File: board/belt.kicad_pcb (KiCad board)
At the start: 2 copper layers, 56.5 x 48.2 mm, 25 parts, among them J1 USB_B_Micro, J2 USB_B_Micro, J3 USB_B_Micro, J4 USB_B_Micro, P1 3352T-1-103LF, Q1 BSS138, Q2 BSS138, SW1 SW_SPST, SW2 SW_Push, U1 Teensy4.0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

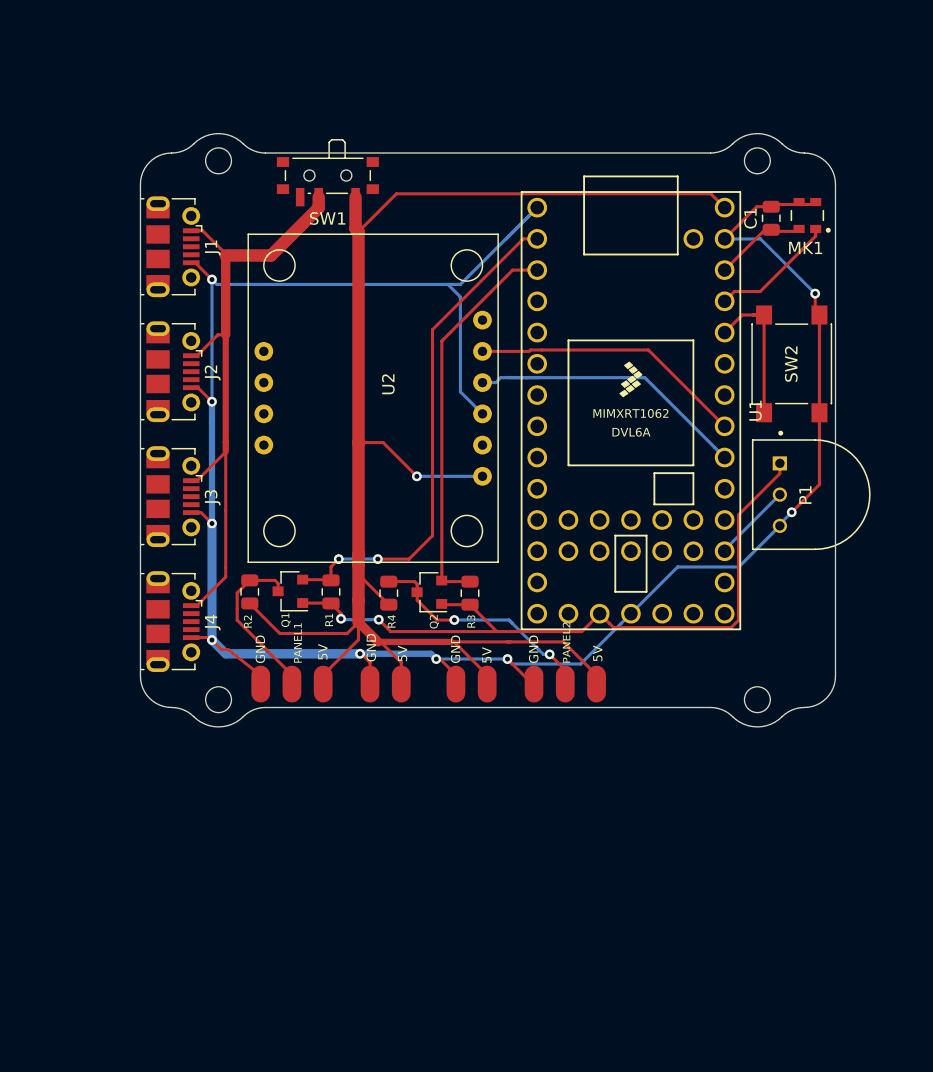
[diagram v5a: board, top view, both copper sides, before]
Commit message: mostly done with next board iteration, except for new microphone; use new microphone in software to draw a rainbow fft that is super fun to play with
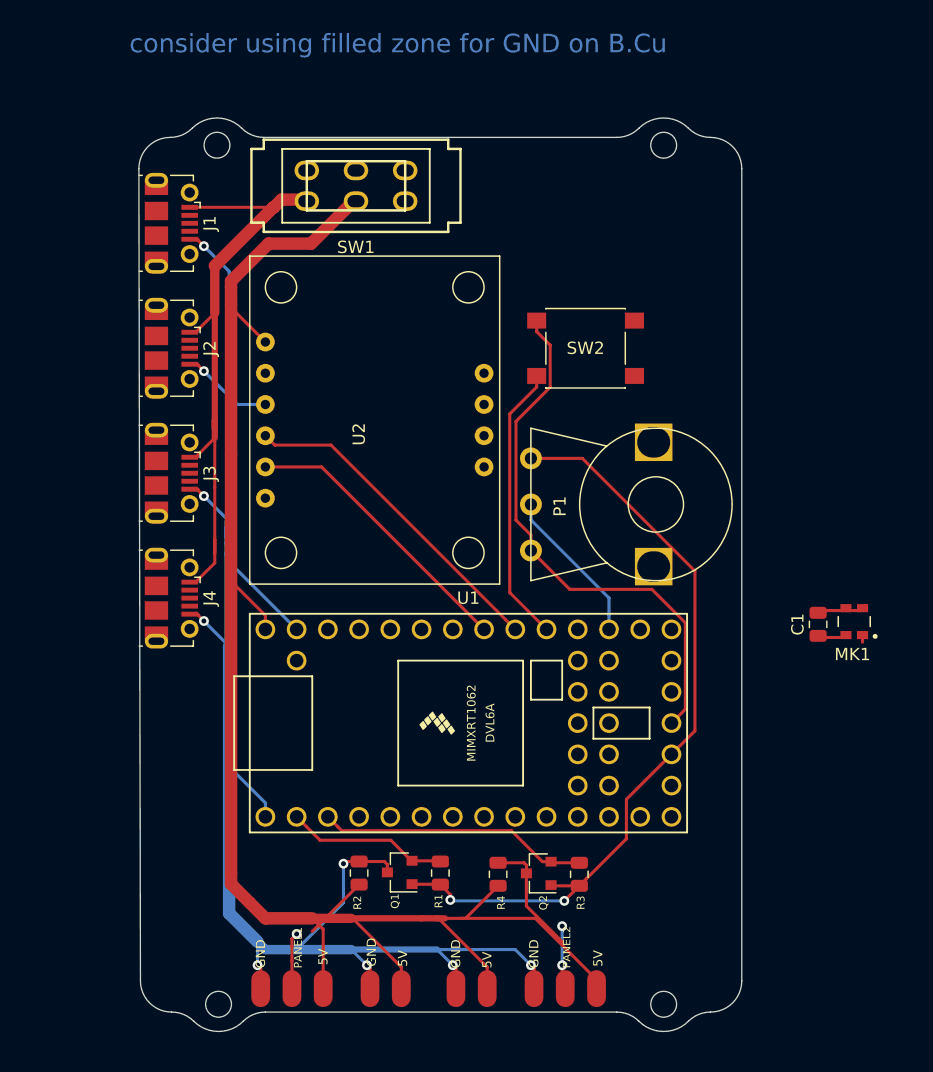
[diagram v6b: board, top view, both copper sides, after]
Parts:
- removed the REF** at (169.5, 70.5)
- removed the REF** at (125.7, 70.5)
- removed the REF** at (125.7, 114.3)
- added REF**: MountingHole_2.1mm, MountingHole:MountingHole_2.1mm, F.Cu at (161.9, 69.2)
- added REF**: MountingHole_2.1mm, MountingHole:MountingHole_2.1mm, F.Cu at (125.6, 69.2)
- added REF**: MountingHole_2.1mm, MountingHole:MountingHole_2.1mm, F.Cu at (125.7, 139.1)
- P1: footprint 3352T-1-103LF:TRIM_3352T-1-103LF -> Potentiometer_THT:PDB12-H
- SW1: value SW_SPST -> SW_DPDT; footprint Button_Switch_SMD:SW_SPDT_PCM12 -> engstad:slide-switch-MFS201N-9-Z
- moved C1 33.2 mm to (174.5, 108.2)
- moved MK1 33.2 mm to (177.4, 108.0)
- moved U1 28.6 mm to (146.1, 116.2), turned to 0 degrees
- moved REF** 25.9 mm to (161.9, 139.1)
- moved PANEL1 24.8 mm to (131.7, 137.8)
- moved PANEL2 24.8 mm to (153.9, 137.8)
- moved PANEL_PWR1 24.8 mm to (139.3, 137.8)
- moved PANEL_PWR2 24.8 mm to (146.3, 137.8)
- moved R3 24.5 mm to (155.1, 128.5)
- moved Q1 24.5 mm to (140.5, 128.3)
- moved Q2 24.5 mm to (151.8, 128.4)
- moved R4 24.5 mm to (148.5, 128.5)
- moved R1 24.5 mm to (143.8, 128.4)
- moved R2 24.5 mm to (137.2, 128.4)
- moved P1 23.1 mm to (151.1, 98.4)
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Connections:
- C1 pad 1: /MIC_PWR -> +3V3
- MK1 pad 4: /MIC_PWR -> +3V3
- SW1 pad 1: VDD -> VBUS
- SW1 pad 2: VBUS -> VDD
- SW1 pad 3: (no net) -> Net-(SW1-Pad3)
- U1 pad 21: Net-(U1-Pad21) -> /MICROPHONE
- U1 pad 24: Net-(U1-Pad24) -> /BUTTON
- U1 pad 29: /BUTTON -> Net-(U1-Pad29)
- U1 pad 30: /MICROPHONE -> Net-(U1-Pad30)
- U1 pad 31: /MIC_PWR -> Net-(U1-Pad31)
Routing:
- net /DATA1: track 41.2 -> 13.3 mm, vias 2 -> 0
- net VDD: track 129.2 -> 139.5 mm, vias 1 -> 0
- net /BUTTON: track 12.7 -> 22.8 mm
- net /DATA2: track 32.1 -> 22.1 mm
- net /MICROPHONE: track 10.2 -> 0.58 mm
- net +3V3: track 57.7 -> 66.1 mm
- net /MIC_PWR: track 7.38 -> 0.00 mm
- net /THUMBDIAL: track 6.46 -> 12.8 mm
- net Net-(PANEL1-Pad2): track 13.8 -> 18.7 mm, vias 0 -> 2
- net Net-(PANEL2-Pad2): track 19.3 -> 16.1 mm
- net /MOTION_SDA: track 25.1 -> 26.8 mm
- net VBUS: track 51.6 -> 53.3 mm
- net /MOTION_SCL: track 22.3 -> 23.3 mm
- net GND: track 186.4 -> 187.3 mm, vias 9 -> 8
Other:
- board size 56.5 x 48.2 mm -> 49 x 74.3 mm
- board text added: "consider using filled zone for GND on B.Cu"

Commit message: checkpoint for 3rd board layout with veritcal structure, two pots, and digital mic
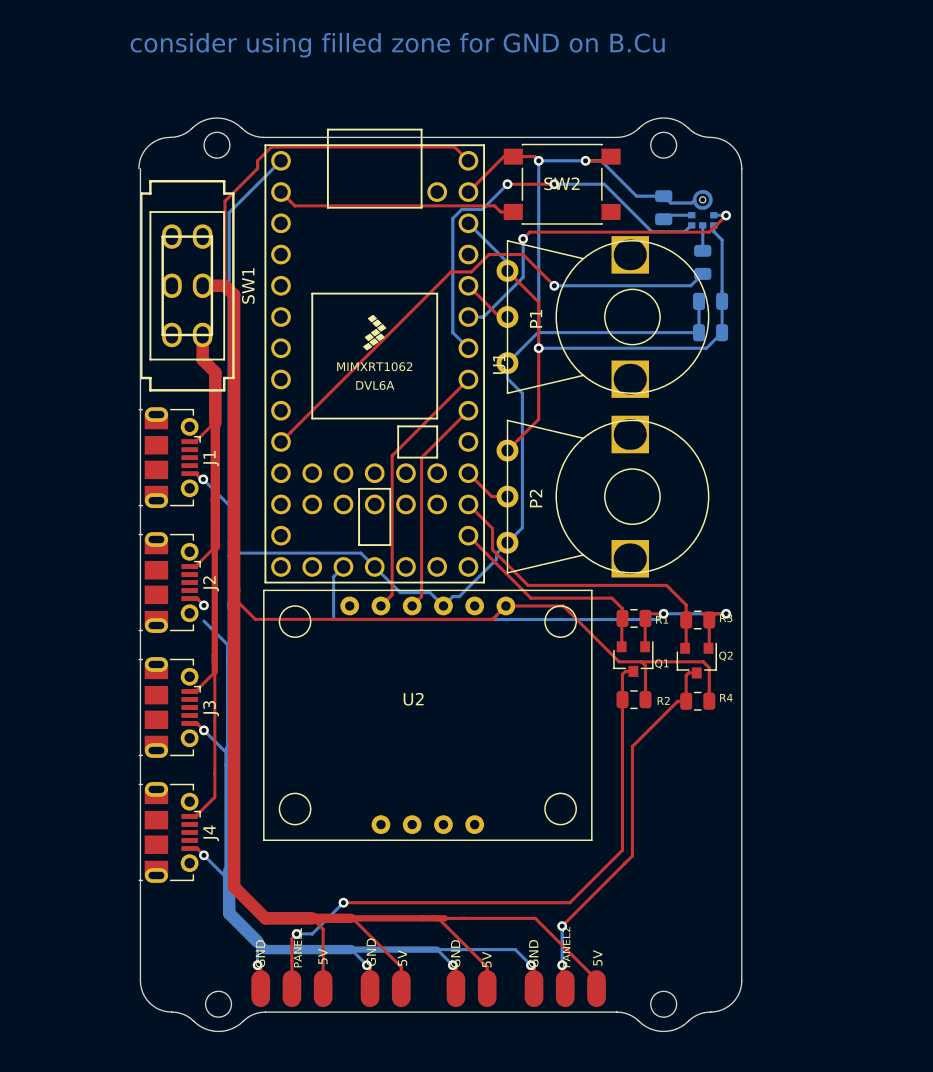
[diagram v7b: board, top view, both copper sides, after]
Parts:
- added C2: 220pF, Capacitor_SMD:C_0805_2012Metric, B.Cu at (165.7, 84.5)
- added P2: 3352T-1-103LF, Potentiometer_THT:PDB12-H, F.Cu at (149.2, 97.8)
- added R5: 10K, Resistor_SMD:R_0805_2012Metric, B.Cu at (161.9, 74.3)
- added R6: 68, Resistor_SMD:R_0805_2012Metric, B.Cu at (165.1, 78.7)
- C1: value 0.1µF -> 1uF; moved to B.Cu
- MK1: value SPW2430HR5H-B -> SPH0645LM4H-B; footprint SPW2430HR5H-B:MIC_SPW2430HR5H-B -> Mic-SPH0645LM4H-B:MIC_SPH0645LM4H-B; moved to B.Cu
- moved MK1 36.4 mm to (165.1, 73.7), turned to 0 degrees
- moved U1 30.2 mm to (138.4, 87.0), turned to 270 degrees
- moved C1 27.7 mm to (165.7, 81.9), turned to 0 degrees
- moved R2 26.4 mm to (159.5, 114.3), turned to 180 degrees
- moved R1 26.0 mm to (159.5, 107.7), turned to 180 degrees
- moved Q1 25.7 mm to (159.5, 111.0), turned to 270 degrees
- moved U2 24.5 mm to (142.9, 115.6), turned to 180 degrees
- moved R3 22.8 mm to (164.7, 107.8), turned to 180 degrees
- moved Q2 21.5 mm to (164.6, 111.1), turned to 270 degrees
- moved R4 21.5 mm to (164.7, 114.4), turned to 180 degrees
- moved J2 19.1 mm to (121.9, 104.8)
- moved J1 19.0 mm to (121.9, 94.6)
- moved J3 19.0 mm to (121.9, 114.9)
- moved J4 19.0 mm to (121.9, 125.1)
- moved SW1 15.9 mm to (123.2, 80.6), turned to 90 degrees
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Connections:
- C1 pad 1: +3V3 -> GND
- C1 pad 2: GND -> +3.3VA
- MK1 pad 1: /MICROPHONE -> /MIC_LRCLK
- MK1 pad 2: GND -> Net-(MK1-Pad2)
- MK1 pad 4: +3V3 -> /MIC_BCLK
- P1 pad 1: +3V3 -> +3.3VA
- P1 pad 2: /THUMBDIAL -> /THUMBDIAL1
- U1 pad 10: Net-(U1-Pad10) -> /MIC_DATA_IN
- U1 pad 2: /DATA1 -> /BUTTON
- U1 pad 21: /MICROPHONE -> /DATA1
- U1 pad 22: /THUMBDIAL -> /DATA2
- U1 pad 23: Net-(U1-Pad23) -> /THUMBDIAL2
- U1 pad 24: /BUTTON -> Net-(U1-Pad24)
- U1 pad 27: Net-(U1-Pad27) -> /MIC_LRCLK
- U1 pad 28: Net-(U1-Pad28) -> /MIC_BCLK
- U1 pad 29: Net-(U1-Pad29) -> /THUMBDIAL1
- U1 pad 3: /DATA2 -> Net-(U1-Pad3)
- U1 pad 31: Net-(U1-Pad31) -> +3.3VA
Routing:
- net +3.3VA: track 0.00 -> 46.3 mm, vias 0 -> 1
- net VDD: track 139.5 -> 185.1 mm
- net /MIC_DATA_IN: track 0.00 -> 42.1 mm, vias 0 -> 1
- net GND: track 187.3 -> 225.1 mm, vias 8 -> 10
- net /MIC_LRCLK: track 0.00 -> 33.5 mm, vias 0 -> 2
- net Net-(PANEL1-Pad2): track 18.7 -> 50.0 mm
- net /MIC_BCLK: track 0.00 -> 27.2 mm, vias 0 -> 2
- net +3V3: track 66.1 -> 45.5 mm
- net Net-(PANEL2-Pad2): track 16.1 -> 32.3 mm
- net /THUMBDIAL: track 12.8 -> 0.00 mm
- net /MOTION_SDA: track 26.8 -> 17.8 mm
- net /DATA1: track 13.3 -> 18.3 mm
- net /THUMBDIAL1: track 0.00 -> 4.23 mm
- net /THUMBDIAL2: track 0.00 -> 3.96 mm
- net /DATA2: track 22.1 -> 25.8 mm
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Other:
- outline, holes or cut-outs redrawn

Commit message: new placement for led pads plus a strategy for securing them; tweaks; nearing final design
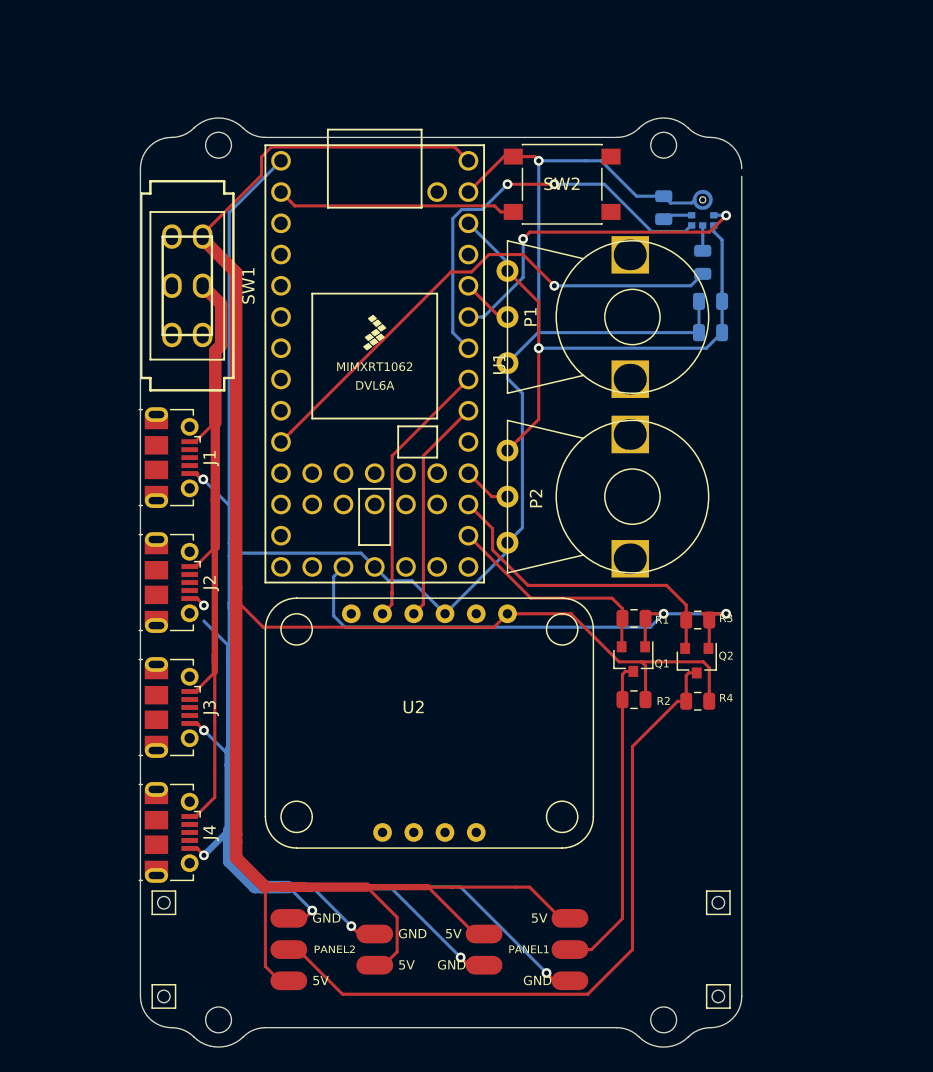
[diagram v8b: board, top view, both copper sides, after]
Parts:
- removed the REF** at (125.7, 139.1)
- removed the REF** at (161.9, 139.1)
- added REF**: TestPoint_THTPad_1.5x1.5mm_Drill0.7mm, TestPoint:TestPoint_THTPad_1.5x1.5mm_Drill0.7mm, F.Cu at (166.4, 130.8)
- added REF**: TestPoint_THTPad_1.5x1.5mm_Drill0.7mm, TestPoint:TestPoint_THTPad_1.5x1.5mm_Drill0.7mm, F.Cu at (166.4, 138.4)
- added REF**: TestPoint_THTPad_1.5x1.5mm_Drill0.7mm, TestPoint:TestPoint_THTPad_1.5x1.5mm_Drill0.7mm, F.Cu at (121.3, 138.4)
- added REF**: TestPoint_THTPad_1.5x1.5mm_Drill0.7mm, TestPoint:TestPoint_THTPad_1.5x1.5mm_Drill0.7mm, F.Cu at (121.3, 130.8)
- added REF**: MountingHole_2.1mm, MountingHole:MountingHole_2.1mm, F.Cu at (125.7, 140.3)
- added REF**: MountingHole_2.1mm, MountingHole:MountingHole_2.1mm, F.Cu at (161.9, 140.3)
- moved PANEL1 22.8 mm to (154.3, 134.6), turned to 270 degrees
- moved PANEL2 22.7 mm to (131.4, 134.6), turned to 90 degrees
- moved PANEL_PWR1 8.61 mm to (147.3, 134.6), turned to 90 degrees
- moved PANEL_PWR2 8.49 mm to (138.4, 134.6), turned to 270 degrees
- moved U2 0.64 mm to (142.9, 116.2)
- moved REF** 0.13 mm to (125.7, 69.2)
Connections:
- SW1 pad 1: VBUS -> Net-(SW1-Pad1)
- SW1 pad 2: VDD -> VBUS
- SW1 pad 3: Net-(SW1-Pad3) -> VDD
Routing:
- net Net-(PANEL2-Pad2): track 32.3 -> 56.8 mm, vias 2 -> 0
- net Net-(PANEL1-Pad2): track 50.0 -> 26.7 mm, vias 2 -> 0
- net GND: track 225.1 -> 231.9 mm, vias 10 -> 9
- net VBUS: track 52.2 -> 56.6 mm
- net VDD: track 185.1 -> 183.6 mm
- net /MOTION_SCL: track 21.4 -> 22.2 mm
- net /MOTION_SDA: track 17.8 -> 18.4 mm
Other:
- board size 49 x 74.3 mm -> 48.9 x 75.5 mm
- board text removed: "consider using filled zone for GND on B.Cu"
